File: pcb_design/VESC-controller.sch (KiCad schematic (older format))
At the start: 26 parts, among them J1 GATE_DRIVER_CONN_U, J2 GATE_DRIVER_CONN_V, J3 GATE_DRIVER_CONN_W, J4 micro USB, J5 ACCEL, J6 REGEN, J7 12V, J8 V_BUS, P1 HALL/Encoder, P101 CANBUS, P2 Resolver, P3 PWR_COMM

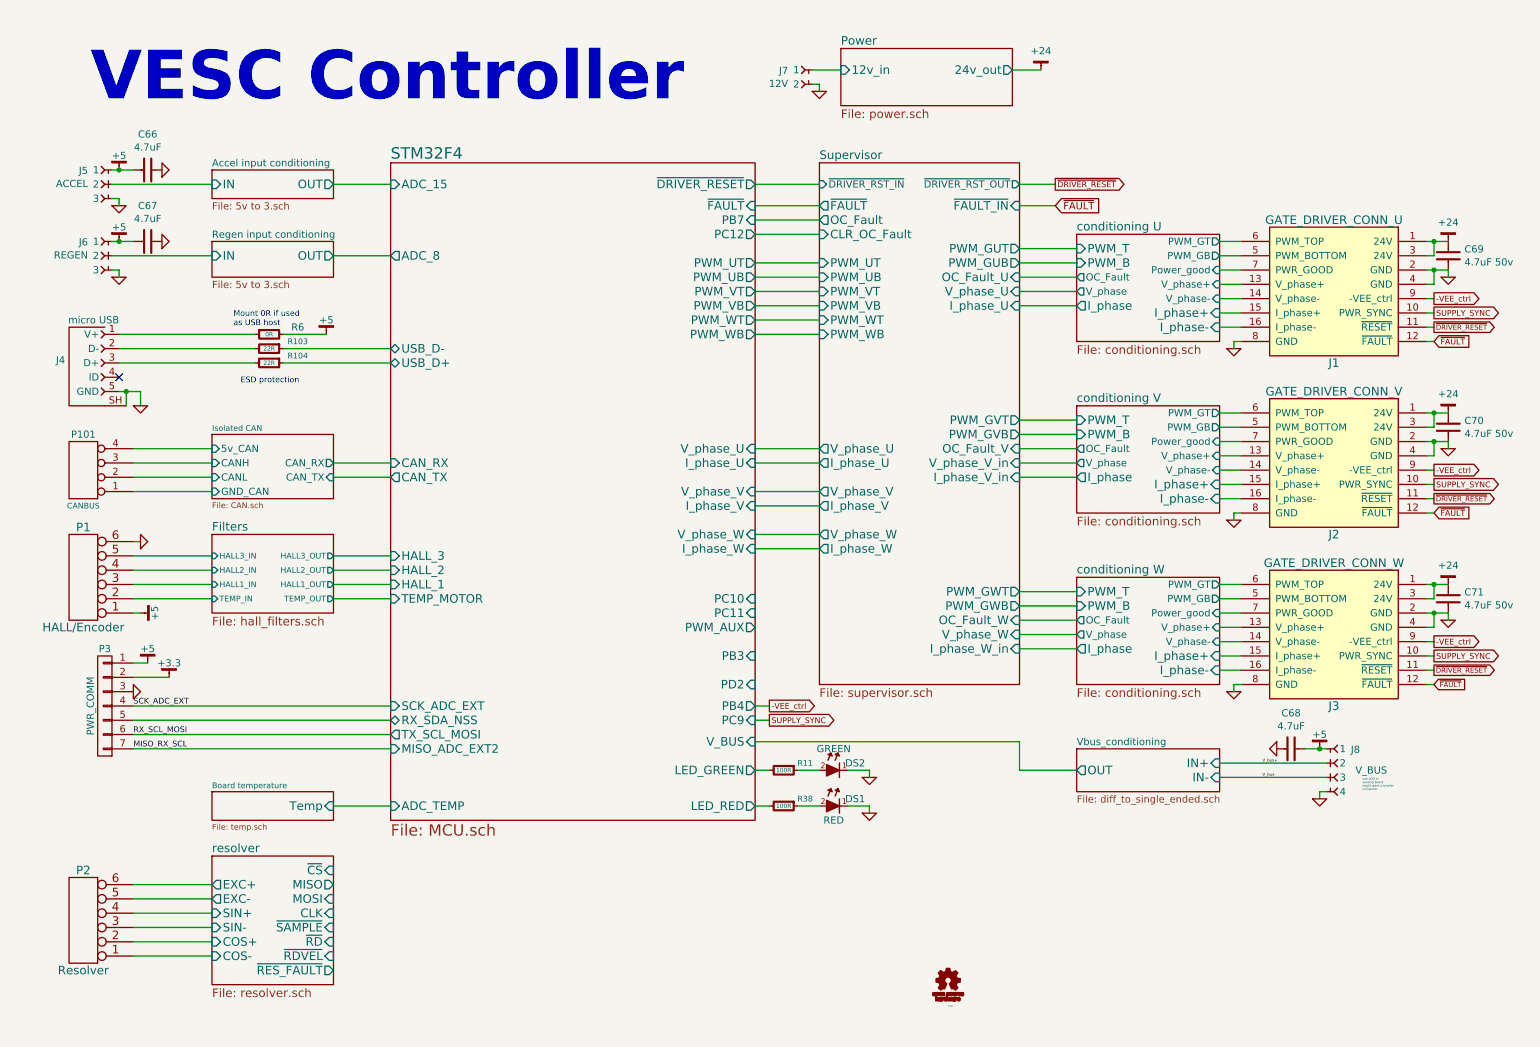
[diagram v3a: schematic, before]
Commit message: Resolver routed. Added 12v regulator. The screw terminals were backwards(!). Started clearing up DRC markers.
Signed-off-by: Marcos Chaparro <mchaparro@paltatech.com>
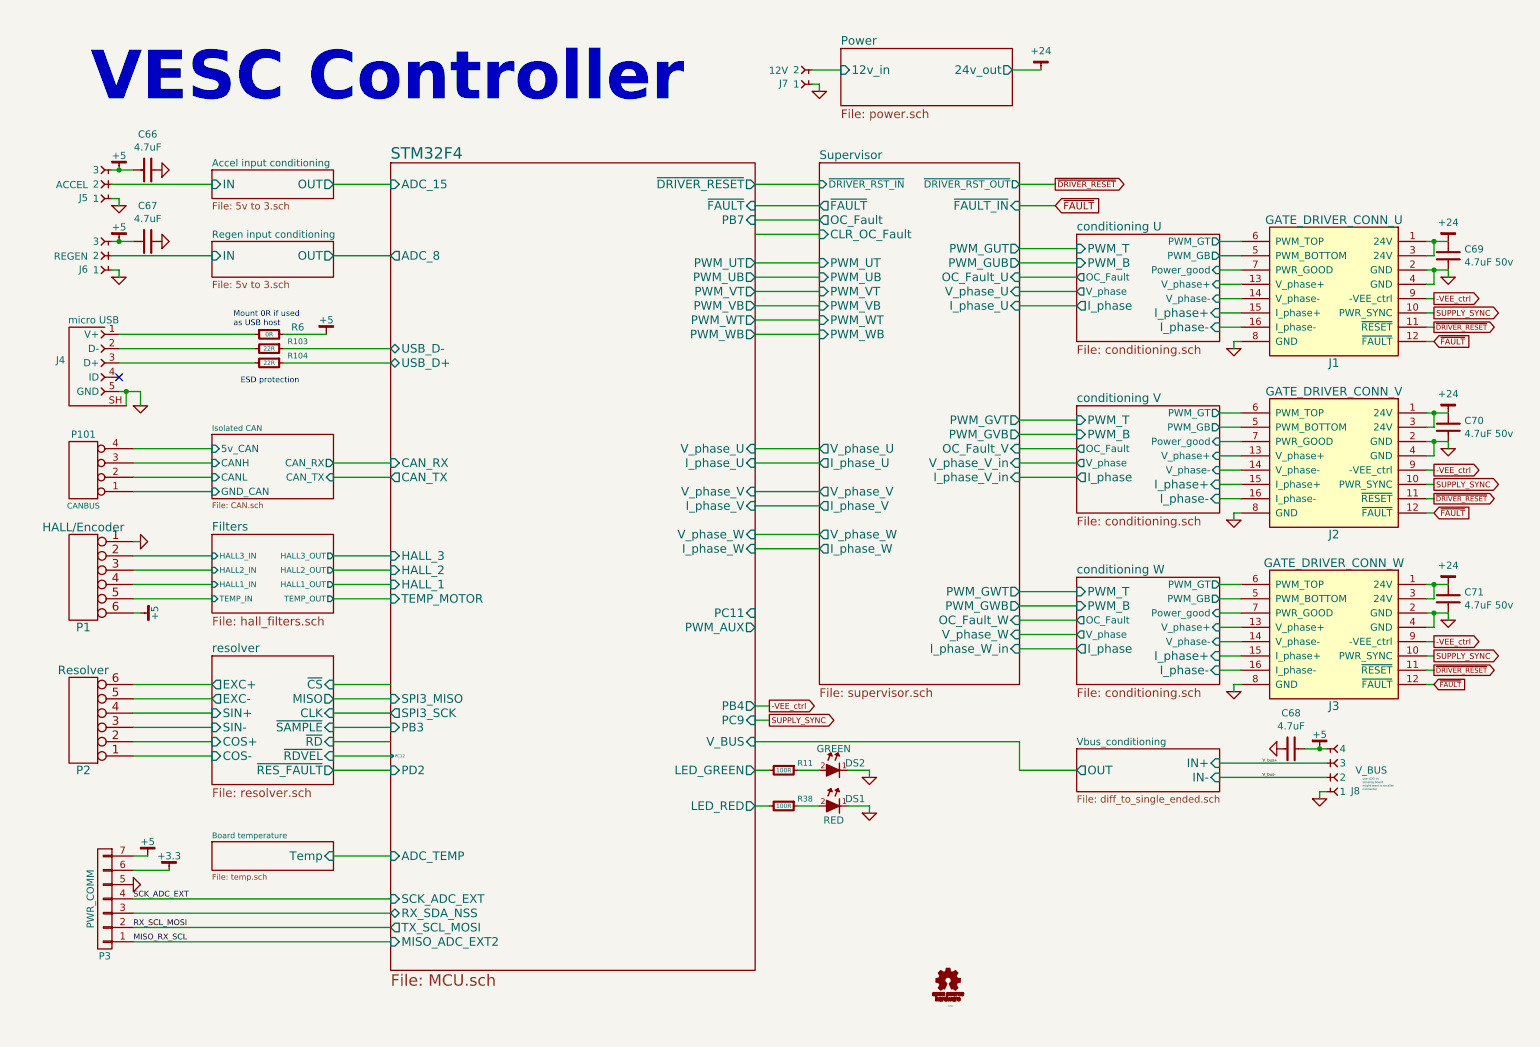
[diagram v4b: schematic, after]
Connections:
- net +3.3: now also P3.6 (P6); no longer P3.2 (P2)
- net +5: now also J5.3, J6.3, J8.4, P1.6, P3.7 (P7); no longer J5.1, J6.1, J8.1, P1.1, P3.1 (P1)
- net Filters/HALL1_IN: now also P1.4; no longer P1.3
- net Filters/HALL2_IN: now also P1.3; no longer P1.4
- net Filters/HALL3_IN: now also P1.2; no longer P1.5
- net Filters/TEMP_IN: now also P1.5; no longer P1.2
- net GND: now also J5.1, J6.1, J7.1, J8.1, P1.1, P3.5 (P5); no longer J5.3, J6.3, J7.2, J8.4, P1.6, P3.3 (P3)
- net MISO_RX_SCL: now also P3.1 (P1); no longer P3.7 (P7)
- net Power/12v_in: now also J7.2; no longer J7.1
- net RX_SCL_MOSI: now also P3.2 (P2); no longer P3.6 (P6)
- net STM32F4/RX_SDA_NSS: now also P3.3 (P3); no longer P3.5 (P5)
- net V_bus+: now also J8.3; no longer J8.2
- net V_bus-: now also J8.2; no longer J8.3
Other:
- moved on the sheet: P2, P3
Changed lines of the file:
@@
 F 3 "" H 1100 4350 60  0001 C CNN
 	1    1100 4350
-	-1   0    0    1
+	-1   0    0    -1
 $EndComp
 $Comp
@@
 L GND-RESCUE-BLDC_4 #PWR02
 U 1 1 522DA0E2
-P 1450 5150
-F 0 "#PWR02" H 1450 5150 30  0001 C CNN
-F 1 "GND" H 1450 5080 30  0001 C CNN
-F 2 "" H 1450 5150 60  0001 C CNN
-F 3 "" H 1450 5150 60  0001 C CNN
-	1    1450 5150
+P 1450 6500
+F 0 "#PWR02" H 1450 6500 30  0001 C CNN
+F 1 "GND" H 1450 6430 30  0001 C CNN
+F 2 "" H 1450 6500 60  0001 C CNN
+F 3 "" H 1450 6500 60  0001 C CNN
+	1    1450 6500
 	0    -1   1    0
 $EndComp
@@
 Text Notes 2200 3000 0    40   ~ 0
 ESD protection\n
-Text Label 1450 5450 0    40   ~ 0
+Text Label 1450 6800 0    40   ~ 0
 RX_SCL_MOSI
-Text Label 1450 5250 0    40   ~ 0
+Text Label 1450 6600 0    40   ~ 0
 SCK_ADC_EXT
 $Sheet
-S 2000 5850 850  200
+S 2000 6200 850  200
 U 53FFB3E2
 F0 "Board temperature" 40
 F1 "temp.sch" 40
-F2 "Temp" I R 2850 5950 60
+F2 "Temp" I R 2850 6300 60
 $EndSheet
 $Sheet
@@
 L CONN_01X07 P3
 U 1 1 55D4F5E0
-P 1250 5250
-F 0 "P3" H 1250 5650 50  0000 C CNN
-F 1 "PWR_COMM" V 1350 5250 50  0000 C CNN
-F 2 "conn-phoenix:mcv_1,5-7-G-3,81" H 1250 5250 60  0001 C CNN
-F 3 "" H 1250 5250 60  0000 C CNN
-	1    1250 5250
-	-1   0    0    -1
+P 1250 6600
+F 0 "P3" H 1250 7000 50  0000 C CNN
+F 1 "PWR_COMM" V 1350 6600 50  0000 C CNN
+F 2 "conn-phoenix:mcv_1,5-7-G-3,81" H 1250 6600 60  0001 C CNN
+F 3 "" H 1250 6600 60  0000 C CNN
+	1    1250 6600
+	-1   0    0    1
 $EndComp
-Text Label 1450 5550 0    40   ~ 0
+Text Label 1450 6900 0    40   ~ 0
 MISO_RX_SCL
 $Comp
@@
 VESC Controller
 Wire Wire Line
-	1550 4950 1450 4950
+	1550 6300 1450 6300
 Wire Wire Line
-	1700 5050 1450 5050
+	1700 6400 1450 6400
 Wire Wire Line
 	1350 3050 1500 3050
@@
 	5800 4150 6250 4150
 Wire Wire Line
-	1450 5450 3250 5450
+	1450 6800 3250 6800
 Wire Wire Line
-	1450 5350 3250 5350
+	1450 6700 3250 6700
 Wire Wire Line
-	1450 5250 3250 5250
+	1450 6600 3250 6600
 Wire Wire Line
 	1450 3650 2000 3650
@@
 	2800 2650 2500 2650
 Wire Wire Line
-	2850 5950 3250 5950
+	2850 6300 3250 6300
 Wire Wire Line
-	3250 5550 1450 5550
+	3250 6900 1450 6900
 Wire Wire Line
 	7650 1600 7900 1600
@@
 	2000 2100 1300 2100
 $Sheet
-S 3250 1450 2550 4600
+S 3250 1450 2550 5650
 U 588A991B
 F0 "STM32F4" 80
@@
 F5 "HALL_2" I L 3250 4300 60
 F6 "HALL_3" I L 3250 4200 60
-F7 "TX_SCL_MOSI" O L 3250 5450 60
+F7 "TX_SCL_MOSI" O L 3250 6800 60
 F8 "TEMP_MOTOR" I L 3250 4500 60
 F9 "PWM_WB" O R 5800 2650 60
 F10 "PWM_VB" O R 5800 2450 60
 F11 "PWM_UB" O R 5800 2250 60
-F12 "SCK_ADC_EXT" I L 3250 5250 60
+F12 "SCK_ADC_EXT" I L 3250 6600 60
 F13 "~FAULT" I R 5800 1750 60
 F14 "PWM_WT" O R 5800 2550 60
@@
 F25 "LED_RED" O R 5800 5950 60
 F26 "LED_GREEN" O R 5800 5700 60
-F27 "MISO_ADC_EXT2" I L 3250 5550 60
-F28 "ADC_TEMP" I L 3250 5950 60
+F27 "MISO_ADC_EXT2" I L 3250 6900 60
+F28 "ADC_TEMP" I L 3250 6300 60
 F29 "I_phase_W" I R 5800 4150 60
 F30 "ADC_15" I L 3250 1600 60
-F31 "PD2" I R 5800 5100 60
-F32 "PB3" I R 5800 4900 60
+F31 "PD2" I L 3250 5700 60
+F32 "PB3" I L 3250 5400 60
 F33 "PB4" O R 5800 5250 60
 F34 "PWM_AUX" O R 5800 4700 60
@@
 F36 "PB7" I R 5800 1850 60
 F37 "PC11" I R 5800 4600 60
-F38 "PC12" O R 5800 1950 60
-F39 "PC10" I R 5800 4500 60
-F40 "PC9" I R 5800 5350 60
-F41 "RX_SDA_NSS" T L 3250 5350 60
-F42 "ADC_8" O L 3250 2100 60
+F38 "PC9" I R 5800 5350 60
+F39 "RX_SDA_NSS" T L 3250 6700 60
+F40 "ADC_8" O L 3250 2100 60
+F41 "SPI3_MISO" I L 3250 5200 60
+F42 "SPI3_SCK" O L 3250 5300 60
+F43 "PC12" I L 3250 5600 20
 $EndSheet
 Text GLabel 5900 5250 2    40   Output ~ 0
@@
 L CONN-100MIL-F-1x3 J5
 U 1 1 588A64D1
-P 1250 1500
-F 0 "J5" H 1368 1495 50  0000 L CNN
-F 1 "ACCEL" H 1368 1404 50  0000 L CNN
-F 2 "conn-phoenix:mcv_1,5-3-G-3,81" H 1250 1500 50  0001 C CNN
-F 3 "" H 1250 1500 50  0000 C CNN
-	1    1250 1500
-	-1   0    0    -1
+P 1250 1700
+F 0 "J5" H 1368 1695 50  0000 L CNN
+F 1 "ACCEL" H 1368 1604 50  0000 L CNN
+F 2 "conn-phoenix:mcv_1,5-3-G-3,81" H 1250 1700 50  0001 C CNN
+F 3 "" H 1250 1700 50  0000 C CNN
+	1    1250 1700
+	-1   0    0    1
 $EndComp
 $Comp
@@
 L CONN-100MIL-F-1x3 J6
 U 1 1 588A919A
-P 1250 2000
-F 0 "J6" H 1368 1995 50  0000 L CNN
-F 1 "REGEN" H 1368 1904 50  0000 L CNN
-F 2 "conn-phoenix:mcv_1,5-3-G-3,81" H 1250 2000 50  0001 C CNN
-F 3 "" H 1250 2000 50  0000 C CNN
-	1    1250 2000
-	-1   0    0    -1
+P 1250 2200
+F 0 "J6" H 1368 2195 50  0000 L CNN
+F 1 "REGEN" H 1368 2104 50  0000 L CNN
+F 2 "conn-phoenix:mcv_1,5-3-G-3,81" H 1250 2200 50  0001 C CNN
+F 3 "" H 1250 2200 50  0000 C CNN
+	1    1250 2200
+	-1   0    0    1
 $EndComp
 Wire Wire Line
@@
 L CONN-100MIL-F-1x2 J7
 U 1 1 588CB398
-P 6150 800
-F 0 "J7" H 6269 795 50  0000 L CNN
-F 1 "12V" H 6269 704 50  0000 L CNN
-F 2 "conn-phoenix:mcv_1,5-2-G-3,81" H 6150 800 50  0001 C CNN
-F 3 "" H 6150 800 50  0000 C CNN
-	1    6150 800
-	-1   0    0    -1
+P 6150 900
+F 0 "J7" H 6269 895 50  0000 L CNN
+F 1 "12V" H 6269 804 50  0000 L CNN
+F 2 "conn-phoenix:mcv_1,5-2-G-3,81" H 6150 900 50  0001 C CNN
+F 3 "" H 6150 900 50  0000 C CNN
+	1    6150 900
+	-1   0    0    1
 $EndComp
 Wire Wire Line
@@
 L +5 #PWR018
 U 1 1 588BE146
-P 1550 4950
-F 0 "#PWR018" H -50 -250 30  0001 C CNN
-F 1 "+5" H 1550 5050 50  0000 C CNN
-F 2 "" H -50 -300 60  0000 C CNN
-F 3 "" H -50 -300 60  0000 C CNN
-	1    1550 4950
+P 1550 6300
+F 0 "#PWR018" H -50 1100 30  0001 C CNN
+F 1 "+5" H 1550 6400 50  0000 C CNN
+F 2 "" H -50 1050 60  0000 C CNN
+F 3 "" H -50 1050 60  0000 C CNN
+	1    1550 6300
 	1    0    0    -1
 $EndComp
@@
 L +3.3 #PWR019
 U 1 1 588BE494
-P 1700 5050
-F 0 "#PWR019" H 50  -200 30  0001 C CNN
-F 1 "+3.3" H 1700 5150 50  0000 C CNN
-F 2 "" H 50  -250 60  0000 C CNN
-F 3 "" H 50  -250 60  0000 C CNN
-	1    1700 5050
+P 1700 6400
+F 0 "#PWR019" H 50  1150 30  0001 C CNN
+F 1 "+3.3" H 1700 6500 50  0000 C CNN
+F 2 "" H 50  1100 60  0000 C CNN
+F 3 "" H 50  1100 60  0000 C CNN
+	1    1700 6400
 	1    0    0    -1
 $EndComp
@@
 L CONN-100MIL-F-1x4 J8
 U 1 1 588E0AC7
-P 9850 5550
-F 0 "J8" H 9968 5545 50  0000 L CNN
-F 1 "V_BUS" H 10000 5400 50  0000 L CNN
-F 2 "conn-phoenix:mcv_1,5-4-G-3,81" H 9850 5550 50  0001 C CNN
-F 3 "" H 9850 5550 50  0000 C CNN
-	1    9850 5550
-	1    0    0    -1
+P 9850 5850
+F 0 "J8" H 9968 5845 50  0000 L CNN
+F 1 "V_BUS" H 10000 5700 50  0000 L CNN
+F 2 "conn-phoenix:mcv_1,5-4-G-3,81" H 9850 5850 50  0001 C CNN
+F 3 "" H 9850 5850 50  0000 C CNN
+	1    9850 5850
+	1    0    0    1
 $EndComp
 Wire Wire Line
@@
 L CONN_6 P2
 U 1 1 588DDA44
-P 1100 6750
-F 0 "P2" H 1100 6400 60  0000 C CNN
-F 1 "Resolver" H 1100 7100 60  0000 C CNN
-F 2 "conn-phoenix:mcv_1,5-6-G-3,81" H 1100 6750 60  0001 C CNN
-F 3 "" H 1100 6750 60  0001 C CNN
-	1    1100 6750
+P 1100 5350
+F 0 "P2" H 1100 5700 60  0000 C CNN
+F 1 "Resolver" H 1100 5000 60  0000 C CNN
+F 2 "conn-phoenix:mcv_1,5-6-G-3,81" H 1100 5350 60  0001 C CNN
+F 3 "" H 1100 5350 60  0001 C CNN
+	1    1100 5350
 	-1   0    0    1
 $EndComp
 $Sheet
-S 2000 6300 850  900
+S 2000 4900 850  900
 U 588E957F
 F0 "resolver" 60
 F1 "resolver.sch" 60
-F2 "EXC+" O L 2000 6500 60
-F3 "EXC-" O L 2000 6600 60
-F4 "SIN+" I L 2000 6700 60
-F5 "SIN-" I L 2000 6800 60
-F6 "COS+" I L 2000 6900 60
-F7 "COS-" I L 2000 7000 60
-F8 "~CS" I R 2850 6400 60
-F9 "MISO" O R 2850 6500 60
-F10 "MOSI" I R 2850 6600 60
-F11 "CLK" I R 2850 6700 60
-F12 "~SAMPLE" I R 2850 6800 60
-F13 "~RD" I R 2850 6900 60
-F14 "~RDVEL" I R 2850 7000 60
-F15 "~RES_FAULT" O R 2850 7100 60
+F2 "EXC+" O L 2000 5100 60
+F3 "EXC-" O L 2000 5200 60
+F4 "SIN+" I L 2000 5300 60
+F5 "SIN-" I L 2000 5400 60
+F6 "COS+" I L 2000 5500 60
+F7 "COS-" I L 2000 5600 60
+F8 "~CS" I R 2850 5100 60
+F9 "CLK" I R 2850 5300 60
+F10 "~SAMPLE" I R 2850 5400 60
+F11 "~RD" I R 2850 5500 60
+F12 "~RDVEL" I R 2850 5600 60
+F13 "~RES_FAULT" O R 2850 5700 60
+F14 "MISO" O R 2850 5200 60
 $EndSheet
 Wire Wire Line
-	2000 6500 1450 6500
+	2000 5100 1450 5100
+Wire Wire Line
+	1450 5200 2000 5200
+Wire Wire Line
+	2000 5300 1450 5300
+Wire Wire Line
+	1450 5400 2000 5400
+Wire Wire Line
+	2000 5500 1450 5500
+Wire Wire Line
+	1450 5600 2000 5600
+Wire Wire Line
+	2850 5100 3250 5100
+Wire Wire Line
+	2850 5200 3250 5200
 Wire Wire Line
-	1450 6600 2000 6600
+	2850 5300 3250 5300
 Wire Wire Line
-	2000 6700 1450 6700
+	2850 5400 3250 5400
 Wire Wire Line
-	1450 6800 2000 6800
+	2850 5500 3250 5500
 Wire Wire Line
-	2000 6900 1450 6900
+	2850 5600 3250 5600
 Wire Wire Line
-	1450 7000 2000 7000
+	2850 5700 3250 5700
 $EndSCHEMATC

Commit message: Routing complete. Added 3D models. No DRC errors, a few ERC warnings
Signed-off-by: Marcos Chaparro <mchaparro@paltatech.com>
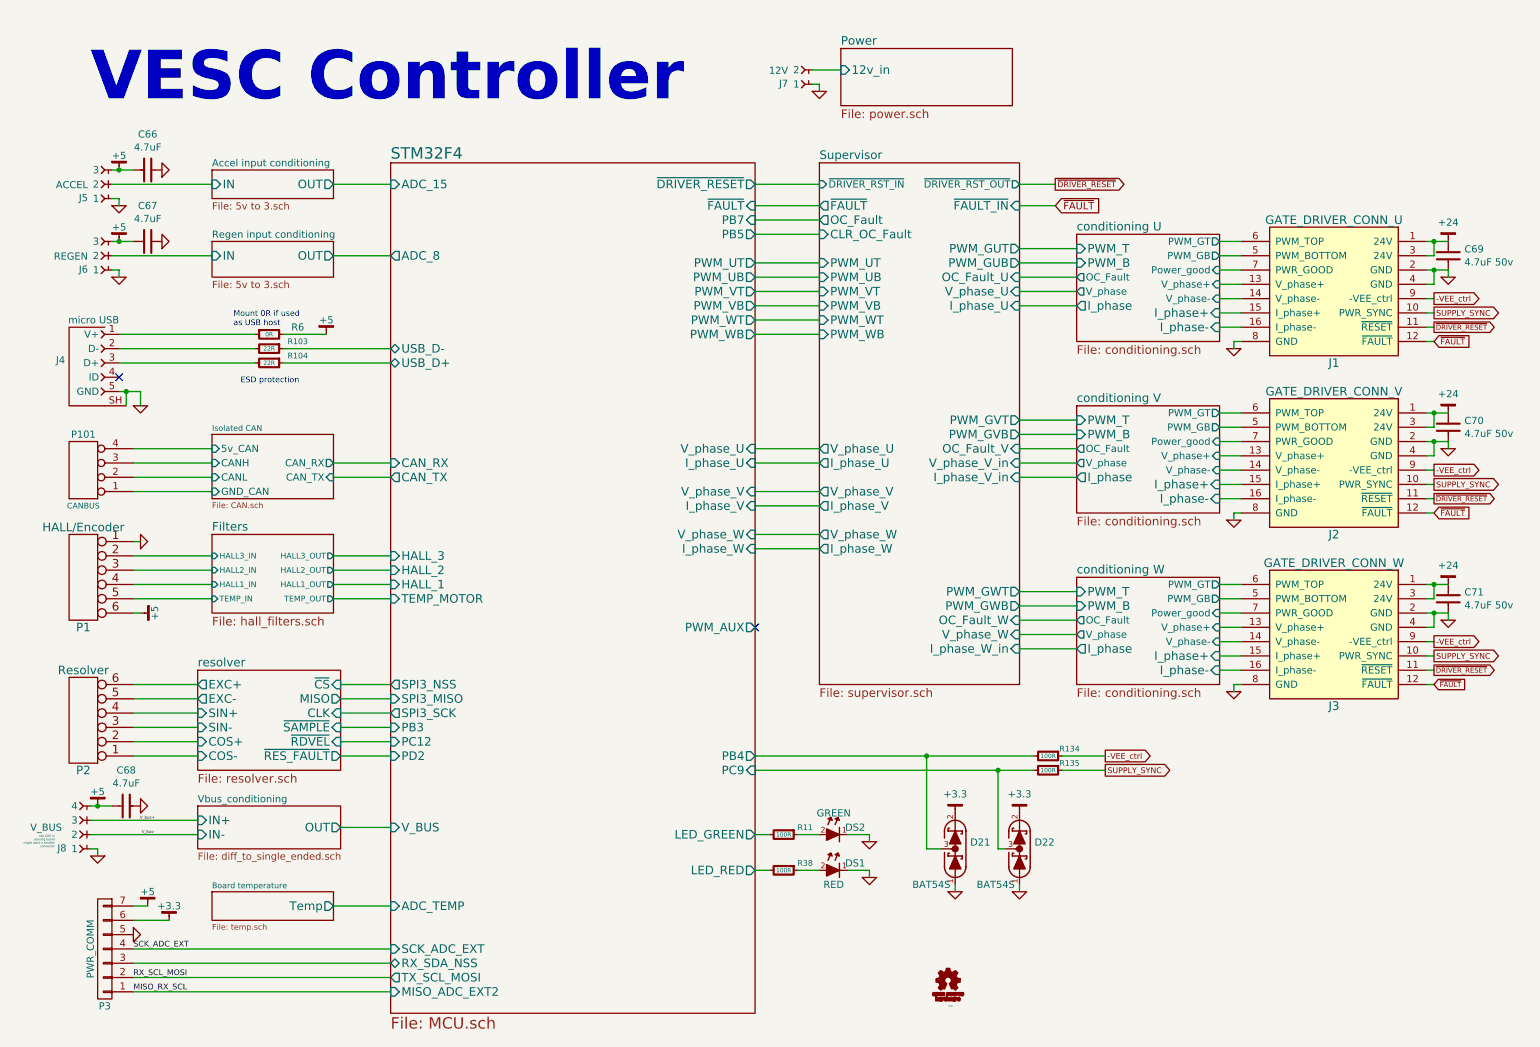
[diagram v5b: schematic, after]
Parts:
- added D21, D22: BAT54S, smd-semi:SOT-23, symbol BAT54S
- added R134, R135: 100R, IPC7351-Nominal:RESC1608X50, symbol R-0603
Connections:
- net +3.3: now also D21.2 (K), D22.2 (K)
- net -VEE_ctrl: now also R134.1
- net GND: now also D21.1 (A), D22.1 (A)
- net SUPPLY_SYNC: now also R135.1
- new net STM32F4/PB4: D21.3 (COM), R134.2
- new net STM32F4/PC9: D22.3 (COM), R135.2
- no-connect marks 1 -> 2
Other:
- moved on the sheet: C68, DS1, DS2, J8, P3, R11, R38

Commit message: Moved references
Signed-off-by: Marcos Chaparro <mchaparro@paltatech.com>
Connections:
- net MISO_RX_SCL renamed STM32F4/MISO_ADC_EXT2
- net RX_SCL_MOSI renamed STM32F4/TX_SCL_MOSI
- net SCK_ADC_EXT renamed STM32F4/SCK_ADC_EXT
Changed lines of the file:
@@
 Text Notes 2200 3000 0    40   ~ 0
 ESD protection\n
-Text Label 1450 7150 0    40   ~ 0
-RX_SCL_MOSI
-Text Label 1450 6950 0    40   ~ 0
-SCK_ADC_EXT
 $Sheet
 S 2000 6550 850  200
@@
 	-1   0    0    1
 $EndComp
-Text Label 1450 7250 0    40   ~ 0
-MISO_RX_SCL
 $Comp
 L GND #PWR05
